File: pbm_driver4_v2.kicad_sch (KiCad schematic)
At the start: 6 parts, among them J1 Conn_02x10_Odd_Even, J2 Conn_01x10

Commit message: WIP - Updating analog switch
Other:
- sheet Driver ports: added DAC[1..2], LED[1..4], SEL[1..4], SENSE[1..4]; removed DAC, LED, SEL, SENSE
- sheet Power Switch ports: added EN_PWR[1..2], PWR[1..2]; removed EN_PWR, PWR

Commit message: Updated 'Size' property to 'Package' on R & C. Cleaned up switch page.
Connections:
- net EN_PWR1 renamed SPARE1
- net EN_PWR2 renamed SPARE2
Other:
- sheet Power Switch ports: added none; removed EN_PWR[1..2], PWR[1..2]
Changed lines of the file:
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@@
 		)
 	)
-	(bus
+	(wire
 		(pts
-			(xy 111.76 101.6) (xy 127 101.6)
+			(xy 72.39 45.72) (xy 72.39 53.34)
 		)
 		(stroke
@@
 		)
 	)
-	(bus
+	(wire
 		(pts
-			(xy 69.85 101.6) (xy 86.36 101.6)
+			(xy 72.39 53.34) (xy 72.39 58.42)
 		)
 		(stroke
@@
 	(wire
 		(pts
-			(xy 72.39 45.72) (xy 72.39 53.34)
+			(xy 101.6 177.8) (xy 101.6 182.88)
 		)
 		(stroke
@@
 		)
 	)
-	(wire
+	(bus
 		(pts
-			(xy 72.39 53.34) (xy 72.39 58.42)
+			(xy 154.94 106.68) (xy 170.18 106.68)
 		)
 		(stroke
@@
 	(wire
 		(pts
-			(xy 101.6 177.8) (xy 101.6 182.88)
+			(xy 72.39 58.42) (xy 72.39 66.04)
 		)
 		(stroke
@@
 		)
 	)
-	(bus
+	(wire
 		(pts
-			(xy 154.94 106.68) (xy 170.18 106.68)
+			(xy 185.42 58.42) (xy 190.5 58.42)
 		)
 		(stroke
@@
 	(wire
 		(pts
-			(xy 72.39 58.42) (xy 72.39 66.04)
+			(xy 90.17 50.8) (xy 106.68 50.8)
 		)
 		(stroke
@@
 	(wire
 		(pts
-			(xy 185.42 58.42) (xy 190.5 58.42)
+			(xy 90.17 53.34) (xy 95.25 53.34)
 		)
 		(stroke
@@
 		)
 	)
-	(wire
-		(pts
-			(xy 90.17 50.8) (xy 106.68 50.8)
-		)
-		(stroke
-			(width 0)
-			(type default)
-		)
-	)
-	(wire
-		(pts
-			(xy 90.17 53.34) (xy 95.25 53.34)
-		)
-		(stroke
-			(width 0)
-			(type default)
-		)
-	)
-	(label "EN_PWR1"
-		(at 60.96 55.88 0)
-		(effects
-			(font
-				(size 1.27 1.27)
-			)
-			(justify left bottom)
-		)
-	)
 	(label "PWR2"
 		(at 172.72 43.18 0)
@@
 		)
 	)
-	(label "PWR[1..2]"
-		(at 125.73 101.6 180)
-		(effects
-			(font
-				(size 1.27 1.27)
-			)
-			(justify right bottom)
-		)
-	)
-	(label "EN_PWR2"
-		(at 106.68 55.88 180)
-		(effects
-			(font
-				(size 1.27 1.27)
-			)
-			(justify right bottom)
-		)
-	)
 	(label "SEL4"
 		(at 106.68 50.8 180)
@@
 		)
 	)
+	(label "SPARE1"
+		(at 60.96 55.88 0)
+		(effects
+			(font
+				(size 1.27 1.27)
+			)
+			(justify left bottom)
+		)
+	)
 	(label "DAC[1..2]"
 		(at 156.21 101.6 0)
@@
 		)
 	)
-	(label "EN_PWR[1..2]"
-		(at 71.12 101.6 0)
-		(effects
-			(font
-				(size 1.27 1.27)
-			)
-			(justify left bottom)
-		)
-	)
 	(label "SENSE3"
 		(at 60.96 43.18 0)
@@
 			)
 			(justify left bottom)
+		)
+	)
+	(label "SPARE2"
+		(at 106.68 55.88 180)
+		(effects
+			(font
+				(size 1.27 1.27)
+			)
+			(justify right bottom)
 		)
 	)
@@
 			)
 		)
-		(pin "EN_PWR[1..2]" input
-			(at 86.36 101.6 180)
-			(effects
-				(font
-					(size 1.27 1.27)
-				)
-				(justify left)
-			)
-		)
-		(pin "PWR[1..2]" output
-			(at 111.76 101.6 0)
-			(effects
-				(font
-					(size 1.27 1.27)
-				)
-				(justify right)
-			)
-		)

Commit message: renamed 'power_switch' schematic sheet to 'power'
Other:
- sheet Power Switch renamed Power
- sheet Power: file sch_power_switch.kicad_sch -> sch_power.kicad_sch
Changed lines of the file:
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@@
 			(color 0 0 0 0.0000)
 		)
-		(property "Sheetname" "Power Switch"
+		(property "Sheetname" "Power"
 			(at 86.36 95.4909 0)
 			(effects
@@
 			)
 		)
-		(property "Sheetfile" "sch_power_switch.kicad_sch"
+		(property "Sheetfile" "sch_power.kicad_sch"
 			(at 86.36 122.5046 0)
 			(effects

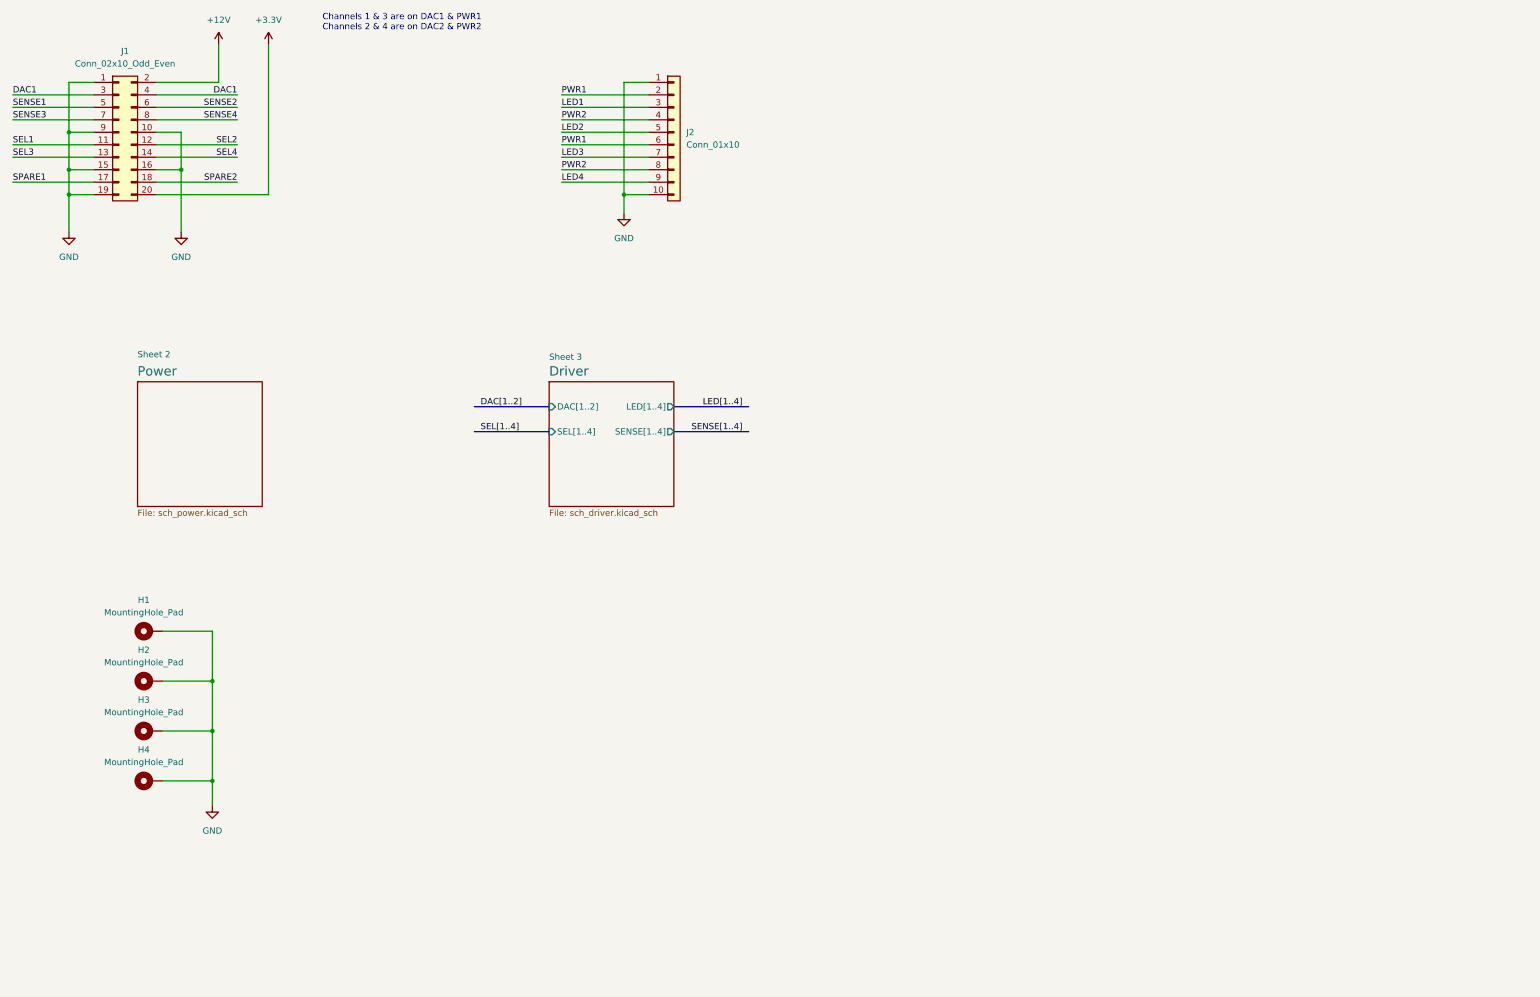
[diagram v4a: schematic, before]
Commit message: Misc schematic cleanup. Fix ERC errors and warnings
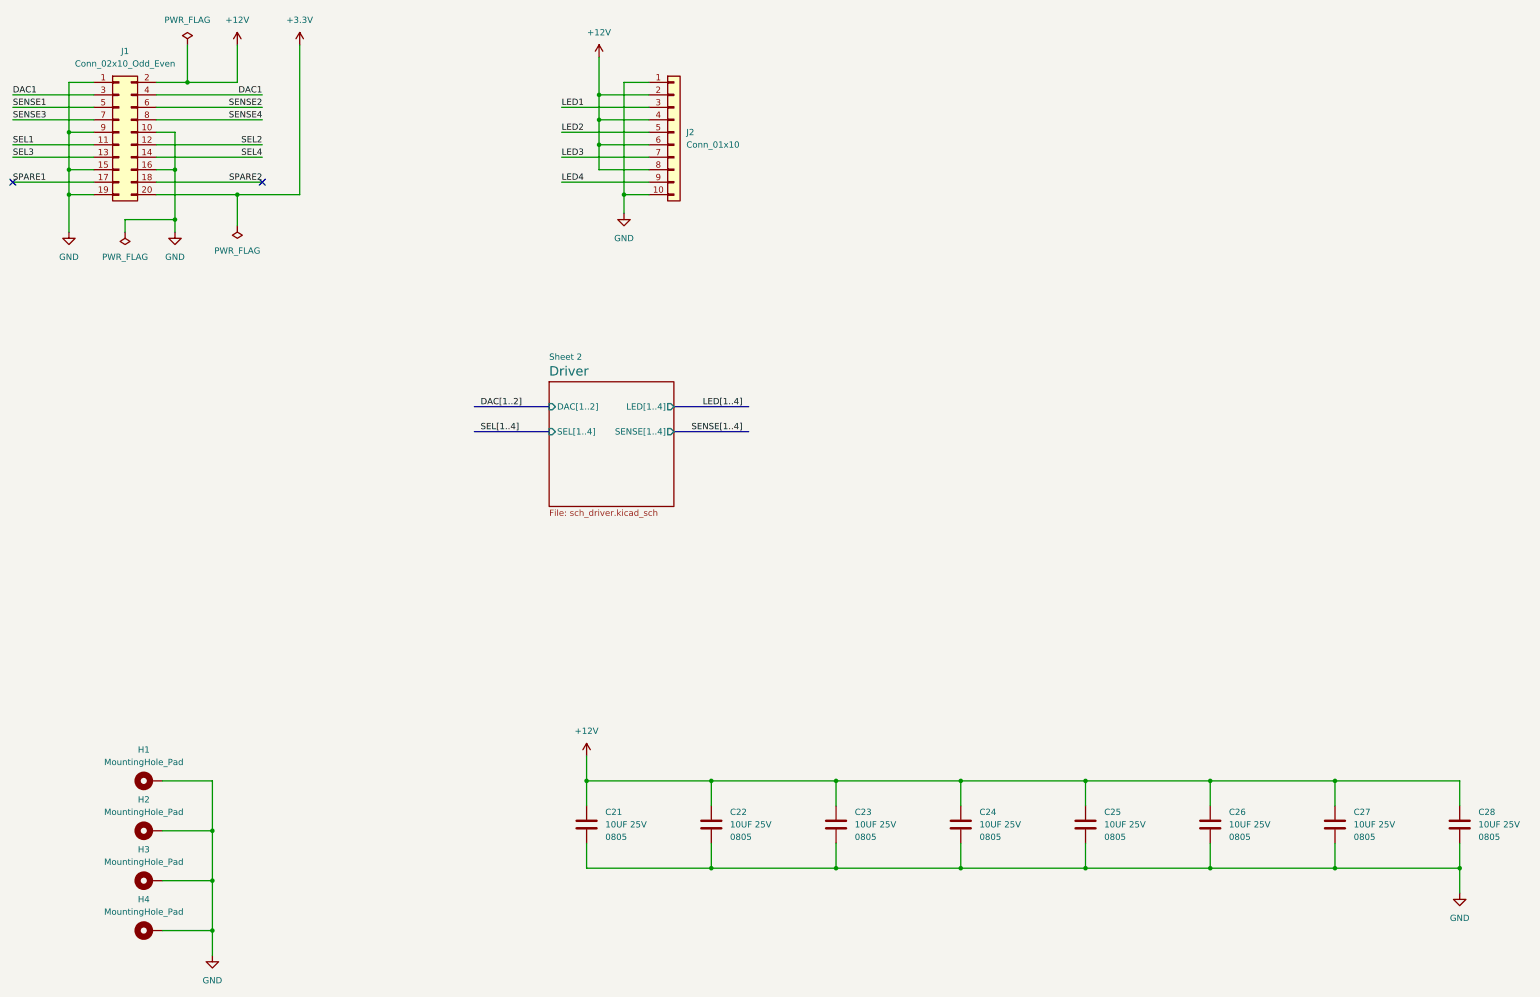
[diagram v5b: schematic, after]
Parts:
- added C21, C22, C23, C24, C25, C26, C27, C28: 10UF 25V, $Local:C_0805_2012Metric, symbol $Local:C_0805_10UF_25V
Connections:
- net PWR1 is gone; now on net +12V: J2.2 (Pin_2), J2.6 (Pin_6)
- net PWR2 is gone; now on net +12V: J2.4 (Pin_4), J2.8 (Pin_8)
- net +12V: now also C21.1, C22.1, C23.1, C24.1, C25.1, C26.1, C27.1, C28.1
- net GND: now also C21.2, C22.2, C23.2, C24.2, C25.2, C26.2, C27.2, C28.2
- no-connect marks 0 -> 2
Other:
- removed sheet Power
- note removed: "Channels 1 & 3 are on DAC1 & PWR1 Channels 2 & 4 are on DAC2 & PWR2"
- moved on the sheet: H1, H2, H3, H4

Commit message: Added active LP filter to sense signals. First pass of part placement on 30x70 mm PCB.
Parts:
- renumbered C21 to C91, C22 to C92, C23 to C93, C24 to C94, C25 to C95, C26 to C96, C27 to C97, C28 to C98
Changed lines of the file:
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@@
 	(generator "eeschema")
 	(generator_version "9.0")
-	(paper "USLedger")
+	(paper "B")
 	(title_block
 		(title "PBM Driver 4 V2")
@@
 		(dnp no)
 		(fields_autoplaced yes)
-		(property "Reference" "C21"
+		(property "Reference" "C91"
 			(at 181.61 184.1499 0)
 			(effects
@@
 			(project "pbm_driver4_v2"
 				(path "/04797749-7aaf-42f7-a5f4-0b9aeb0ad7be"
-					(reference "C21")
+					(reference "C91")
 					(unit 1)
 				)
@@
 		(dnp no)
 		(fields_autoplaced yes)
-		(property "Reference" "C28"
+		(property "Reference" "C98"
 			(at 359.41 184.1499 0)
 			(effects
@@
 			(project "pbm_driver4_v2"
 				(path "/04797749-7aaf-42f7-a5f4-0b9aeb0ad7be"
-					(reference "C28")
+					(reference "C98")
 					(unit 1)
 				)
@@
 		(dnp no)
 		(fields_autoplaced yes)
-		(property "Reference" "C27"
+		(property "Reference" "C97"
 			(at 334.01 184.1499 0)
 			(effects
@@
 			(project "pbm_driver4_v2"
 				(path "/04797749-7aaf-42f7-a5f4-0b9aeb0ad7be"
-					(reference "C27")
+					(reference "C97")
 					(unit 1)
 				)
@@
 		(dnp no)
 		(fields_autoplaced yes)
-		(property "Reference" "C26"
+		(property "Reference" "C96"
 			(at 308.61 184.1499 0)
 			(effects
@@
 			(project "pbm_driver4_v2"
 				(path "/04797749-7aaf-42f7-a5f4-0b9aeb0ad7be"
-					(reference "C26")
+					(reference "C96")
 					(unit 1)
 				)
@@
 		(dnp no)
 		(fields_autoplaced yes)
-		(property "Reference" "C24"
+		(property "Reference" "C94"
 			(at 257.81 184.1499 0)
 			(effects
@@
 			(project "pbm_driver4_v2"
 				(path "/04797749-7aaf-42f7-a5f4-0b9aeb0ad7be"
-					(reference "C24")
+					(reference "C94")
 					(unit 1)
 				)
@@
 		(dnp no)
 		(fields_autoplaced yes)
-		(property "Reference" "C22"
+		(property "Reference" "C92"
 			(at 207.01 184.1499 0)
 			(effects
@@
 			(project "pbm_driver4_v2"
 				(path "/04797749-7aaf-42f7-a5f4-0b9aeb0ad7be"
-					(reference "C22")
+					(reference "C92")
 					(unit 1)
 				)
@@
 		(dnp no)
 		(fields_autoplaced yes)
-		(property "Reference" "C25"
+		(property "Reference" "C95"
 			(at 283.21 184.1499 0)
 			(effects
@@
 			(project "pbm_driver4_v2"
 				(path "/04797749-7aaf-42f7-a5f4-0b9aeb0ad7be"
-					(reference "C25")
+					(reference "C95")
 					(unit 1)
 				)
@@
 		(dnp no)
 		(fields_autoplaced yes)
-		(property "Reference" "C23"
+		(property "Reference" "C93"
 			(at 232.41 184.1499 0)
 			(effects
@@
 			(project "pbm_driver4_v2"
 				(path "/04797749-7aaf-42f7-a5f4-0b9aeb0ad7be"
-					(reference "C23")
+					(reference "C93")
 					(unit 1)
 				)

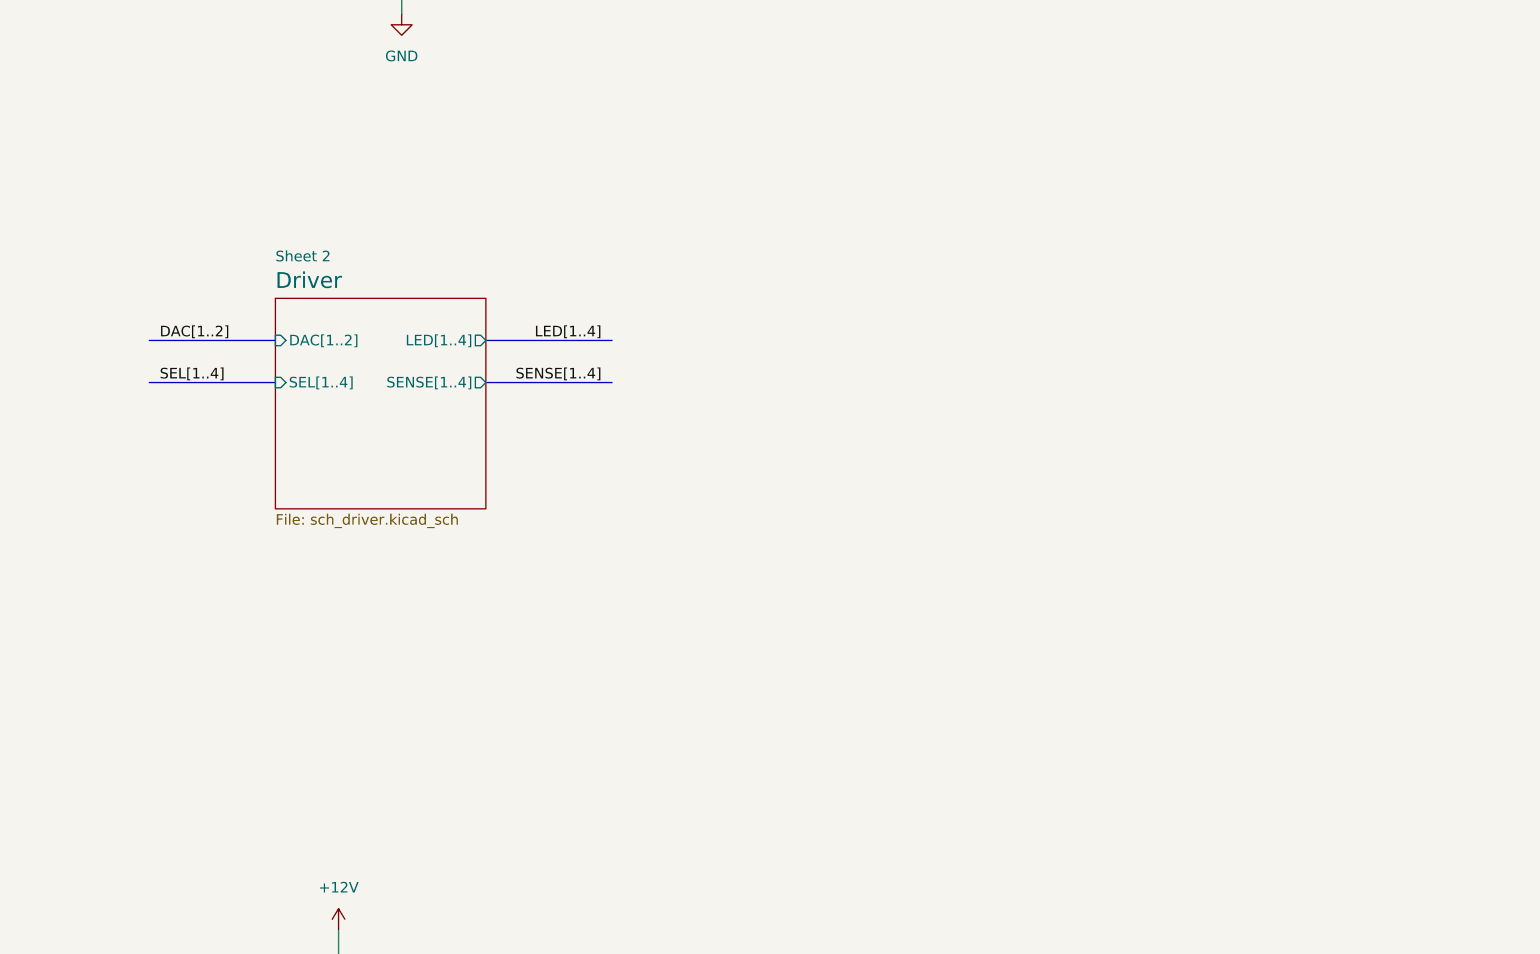
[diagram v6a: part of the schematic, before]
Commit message: Refactor driver schematic sheet into four A-size pages.
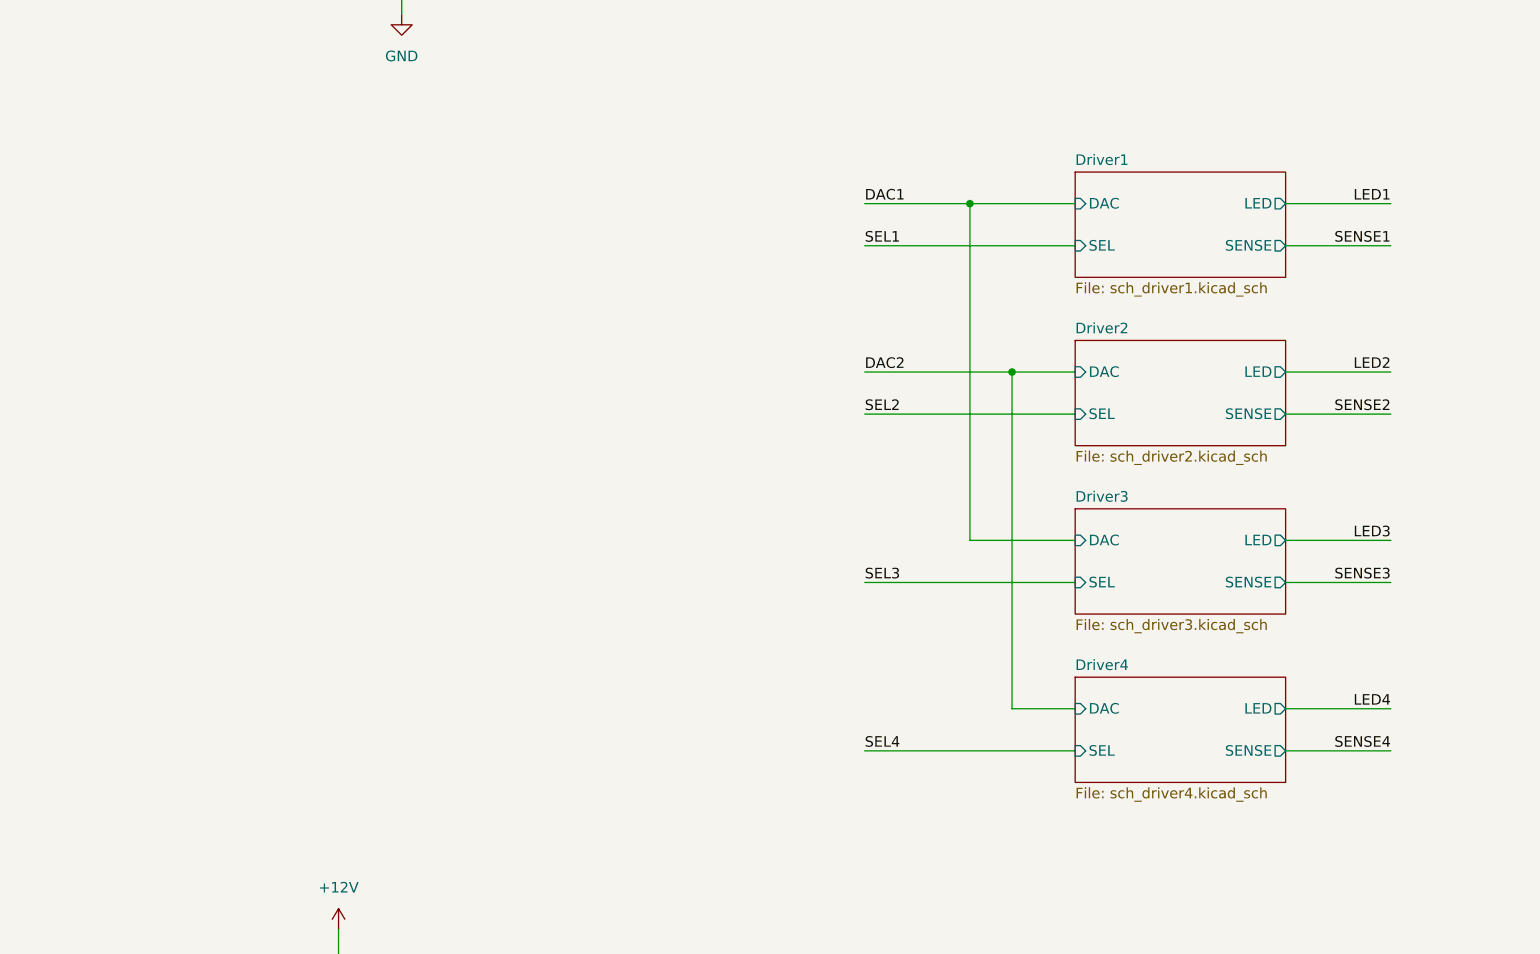
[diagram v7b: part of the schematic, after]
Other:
- removed sheet Driver
- added sheet Driver1 (sch_driver1.kicad_sch)
- added sheet Driver2 (sch_driver2.kicad_sch)
- added sheet Driver3 (sch_driver3.kicad_sch)
- added sheet Driver4 (sch_driver4.kicad_sch)
